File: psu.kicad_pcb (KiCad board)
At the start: 2 copper layers, 76.2 x 76.2 mm, 67 parts, among them J1 Screw_Terminal_01x02, J2 Barrel_Jack, J3 Binding posts, SW1 SW_SP4T, SW2 SW_SP4T, SW3 Lever toggle, U1 LM4040DBZ-2.5, U2 LT3081, U3 LM393, U4 LM334M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

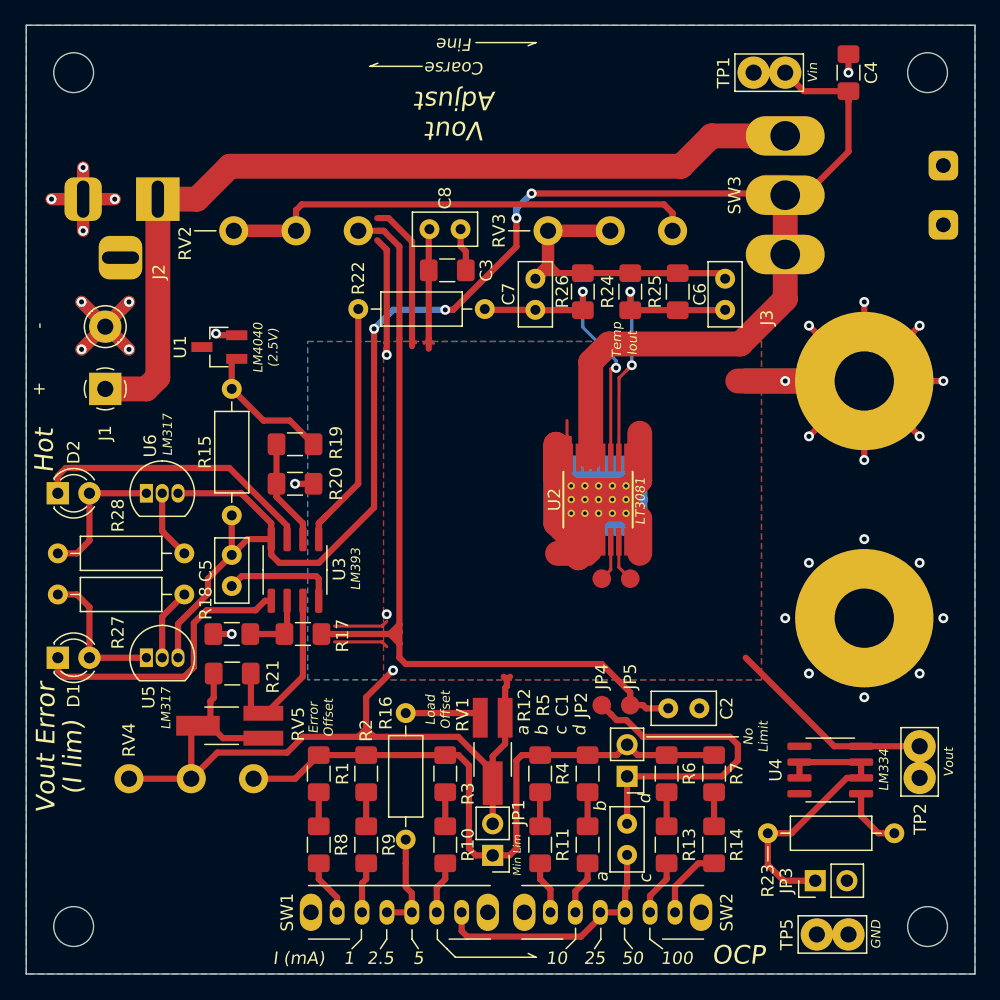
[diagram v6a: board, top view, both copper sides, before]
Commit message: More silkscreen
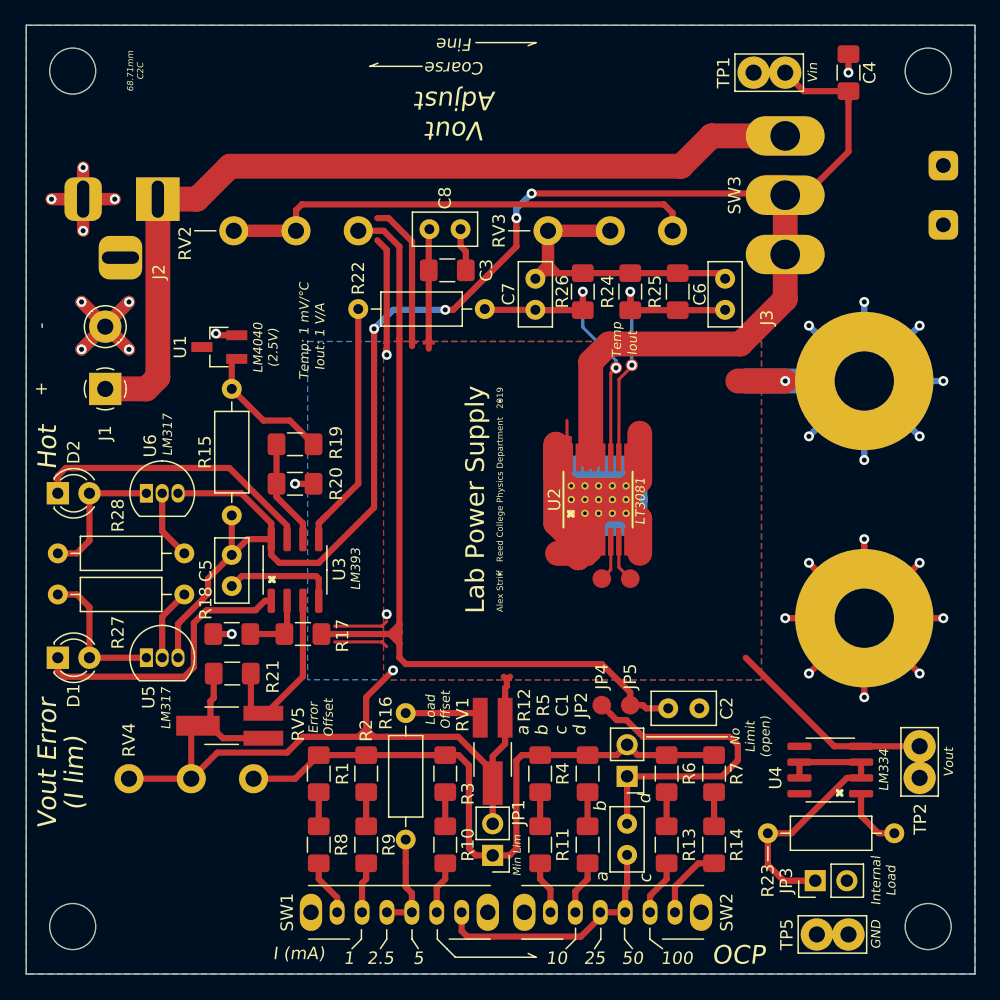
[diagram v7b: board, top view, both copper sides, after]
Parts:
- removed the REF** at (102.9, 132.1)
- removed the REF** at (171.4, 132.1)
- removed the REF** at (171.4, 63.5)
- removed the REF** at (102.9, 63.5)
- added REF**: TestPoint_Pad_D1.0mm, TestPoint:TestPoint_Pad_D1.0mm, F.Cu at (146.4, 87.2)
- added REF**: TestPoint_Pad_D1.0mm, TestPoint:TestPoint_Pad_D1.0mm, F.Cu at (147.7, 87.0)
- added REF**: MountingHole_3.7mm, MountingHole:MountingHole_3.7mm, F.Cu at (171.5, 132.1)
- added REF**: MountingHole_3.7mm, MountingHole:MountingHole_3.7mm, F.Cu at (171.5, 63.4)
- added REF**: MountingHole_3.7mm, MountingHole:MountingHole_3.7mm, F.Cu at (102.8, 63.4)
- added REF**: MountingHole_3.7mm, MountingHole:MountingHole_3.7mm, F.Cu at (102.8, 132.1)
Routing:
- net GND: track 76.2 -> 126.7 mm
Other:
- board text added: "68.71mm C2C"
- board text added: "Alex Striff Reed College Physics Department 2019"
- board text added: "Internal Load"
- board text added: "Iout: 1 V/A"
- board text added: "Lab Power Supply"
- board text added: "No Limit (open)"
- board text added: "Temp: 1 mV/°C"
- board text removed: "No Limit"

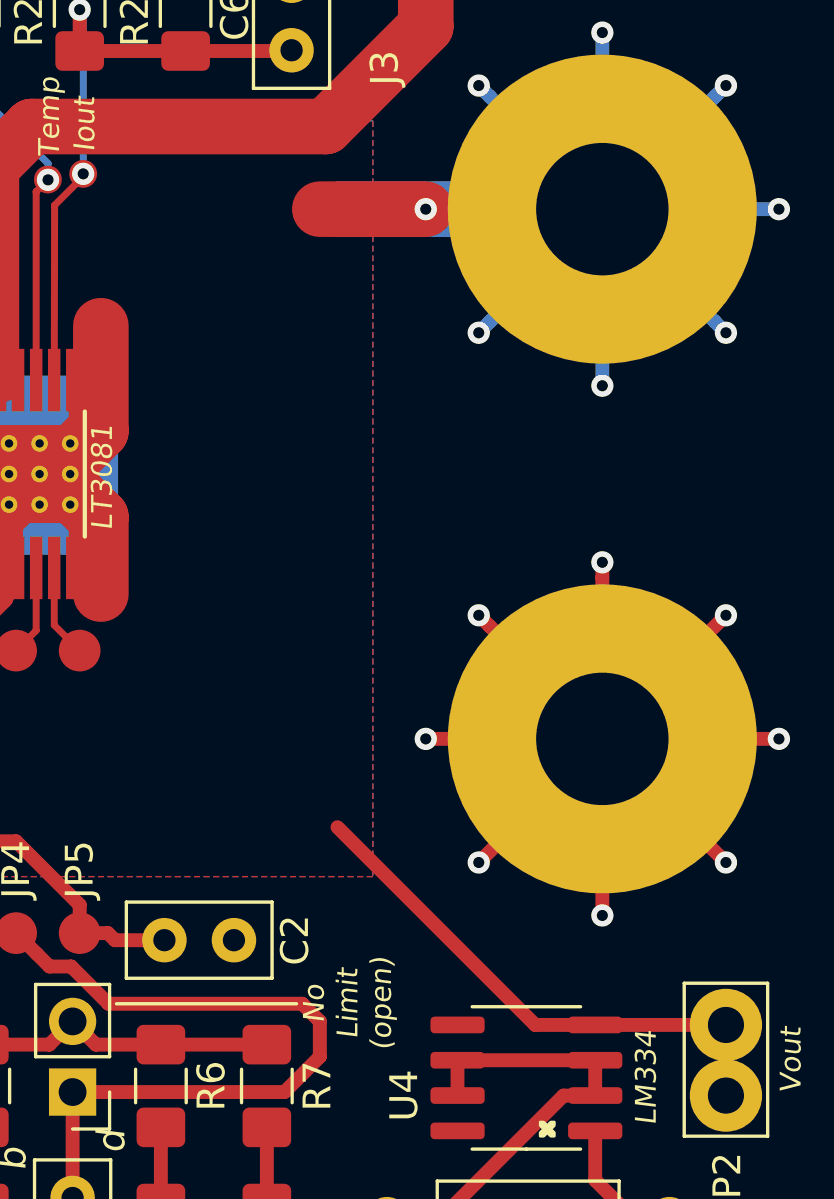
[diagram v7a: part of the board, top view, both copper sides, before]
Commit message: Fixed some 90 degree track-plane junctions
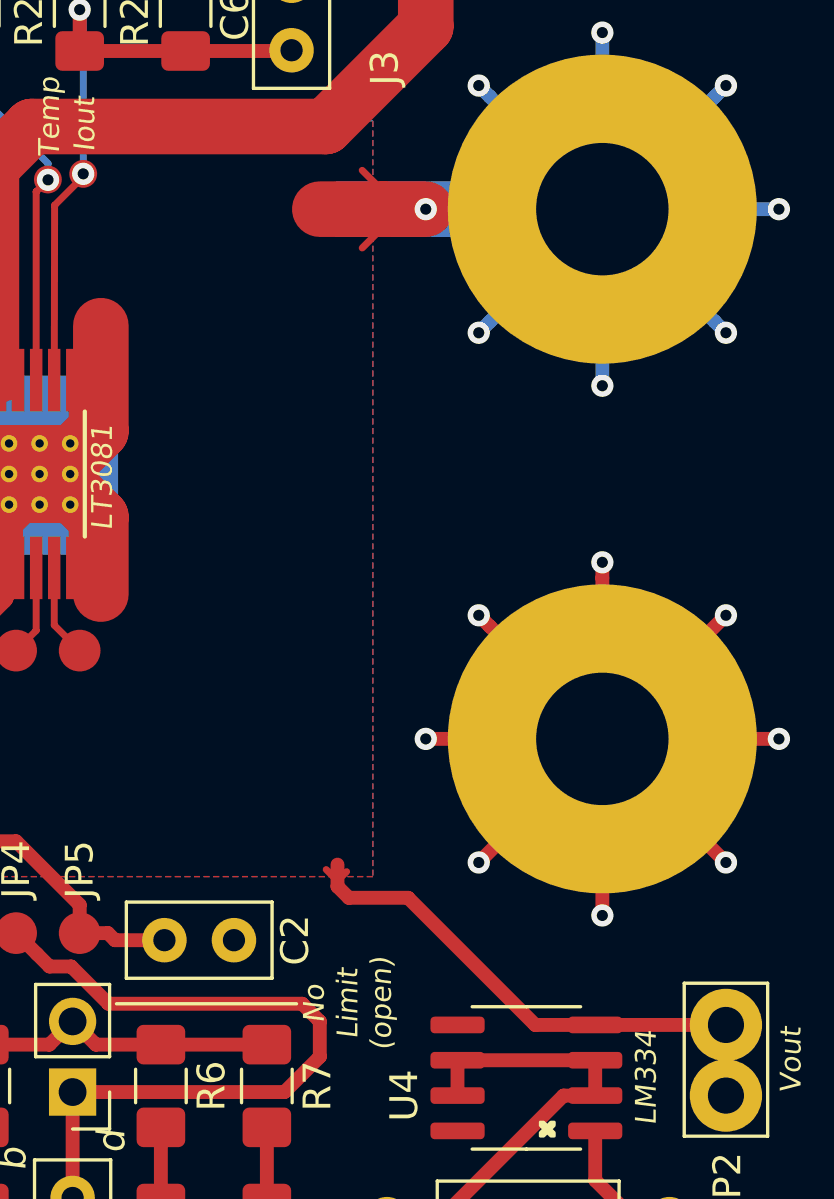
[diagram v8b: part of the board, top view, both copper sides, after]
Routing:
- net Vout: track 308.4 -> 313.0 mm
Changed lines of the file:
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@@
     (thickness 1.6)
     (drawings 86)
-    (tracks 517)
+    (tracks 528)
     (zones 0)
     (modules 69)
@@
   (segment (start 141.605 99.695) (end 143.129 99.695) (width 2) (layer B.Cu) (net 5))
   (segment (start 165.1 88.265) (end 156.845 88.265) (width 2) (layer B.Cu) (net 5))
-  (segment (start 166.113 117.602) (end 163.957 117.602) (width 0.5) (layer F.Cu) (net 5))
-  (segment (start 163.957 117.602) (end 156.845 110.49) (width 0.5) (layer F.Cu) (net 5))
   (via (at 128.016 86.1695) (size 0.8) (drill 0.4) (layers F.Cu B.Cu) (net 5))
   (via (at 128.016 106.9975) (size 0.8) (drill 0.4) (layers F.Cu B.Cu) (net 5))
@@
   (segment (start 112.315 120.2055) (end 112.315 116.4915) (width 0.5) (layer F.Cu) (net 5))
   (segment (start 107.315 120.2055) (end 112.315 120.2055) (width 0.5) (layer F.Cu) (net 5))
-  (segment (start 160.02 88.265) (end 156.21 88.265) (width 2) (layer F.Cu) (net 5))
   (segment (start 128.016 86.1695) (end 128.016 77.978) (width 0.5) (layer F.Cu) (net 5))
   (segment (start 128.016 77.978) (end 128.016 77.724) (width 0.5) (layer F.Cu) (net 5))
@@
   (segment (start 170.815 92.71) (end 170.415001 92.310001) (width 0.5) (layer B.Cu) (net 5))
   (segment (start 172.72 88.265) (end 166.37 88.265) (width 0.5) (layer B.Cu) (net 5))
+  (segment (start 158.496 88.265) (end 158.496 87.63) (width 0.25) (layer F.Cu) (net 5))
+  (segment (start 158.496 88.265) (end 156.21 88.265) (width 2) (layer F.Cu) (net 5))
+  (segment (start 160.02 88.265) (end 158.496 88.265) (width 2) (layer F.Cu) (net 5))
+  (segment (start 158.496 87.63) (end 157.734 86.868) (width 0.25) (layer F.Cu) (net 5))
+  (segment (start 158.496 88.265) (end 158.496 88.9) (width 0.25) (layer F.Cu) (net 5))
+  (segment (start 158.496 88.9) (end 157.734 89.662) (width 0.25) (layer F.Cu) (net 5))
+  (segment (start 159.385 113.03) (end 157.2514 113.03) (width 0.5) (layer F.Cu) (net 5))
+  (segment (start 166.113 117.602) (end 163.957 117.602) (width 0.5) (layer F.Cu) (net 5))
+  (segment (start 163.957 117.602) (end 159.385 113.03) (width 0.5) (layer F.Cu) (net 5))
+  (segment (start 157.2514 113.03) (end 156.845 112.6236) (width 0.5) (layer F.Cu) (net 5))
+  (segment (start 156.845 112.6236) (end 156.845 111.8362) (width 0.5) (layer F.Cu) (net 5))
+  (segment (start 156.845 112.6236) (end 156.845 112.4204) (width 0.25) (layer F.Cu) (net 5))
+  (segment (start 156.845 112.4204) (end 157.1752 112.0902) (width 0.25) (layer F.Cu) (net 5))
+  (segment (start 156.845 112.4204) (end 156.4386 112.014) (width 0.25) (layer F.Cu) (net 5))
   (via (at 139.6492 73.2028) (size 0.8) (drill 0.4) (layers F.Cu B.Cu) (net 6))
   (via (at 127 84.074) (size 0.8) (drill 0.4) (layers F.Cu B.Cu) (net 6))
